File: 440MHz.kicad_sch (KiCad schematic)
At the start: 32 parts, among them J5 BWSMA-KWE-Z001, U7 GRF5604, U9 SKYA21003

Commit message: Finish up inputting things
Signed-off-by: Corey Minyard <corey@minyard.net>
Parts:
- removed C53: 0, Capacitor_SMD:C_0402_1005Metric_Pad0.74x0.62mm_HandSolder, symbol Device:C
- added C38: 5.1pF, Capacitor_SMD:C_0402_1005Metric_Pad0.74x0.62mm_HandSolder, symbol Device:C
- added C68: 2.2pF, Capacitor_SMD:C_0402_1005Metric_Pad0.74x0.62mm_HandSolder, symbol Device:C
- added C69: 0, Capacitor_SMD:C_0402_1005Metric_Pad0.74x0.62mm_HandSolder, symbol Device:C
- added L17: 27nH, Inductor_SMD:L_1210_3225Metric_Pad1.42x2.65mm_HandSolder, symbol Device:L
- added L19: 15nH, Inductor_SMD:L_1210_3225Metric_Pad1.42x2.65mm_HandSolder, symbol Device:L
- C50: value 18pF -> 15pF
- C51: value 18pF -> 5.1pF
- C52: value 33pF -> 2.2pF
- C55, C67: value 680pF -> 100pF
- C57: value 680pF -> 10pF
- C58: value 680pF -> 33pF
- C59, C60, C65: value 12pF -> 1000pF
- C61: value 12pF -> 33pF
- C62: value 12pF -> 2pF
- C63: value 12pF -> 10uF
- C64: value 12pF -> 28pF
- C66: value 12pF -> 1.8pF
- L10: value 47nH -> 43nH
- L11: value 82nH -> 27nH
- L12: value 68nH -> 22nH
- L13: value 68nH -> 10nH
- L14: value 68nH -> 23nH
- L15: value 68nH -> 2.2nH
- R11: value 56K 1% -> 1.96K 1%
- R12: value 56K 1% -> 6.04K 1%
- R13: value 56K 1% -> 0Ω
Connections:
- net 440MHz_RF_P is gone; now on net 440_RX_N: C51.2, L11.1, L9.2
- net 440_RX_P: now also L9.1, C38.1, L17.2
- net 440_TX: now also C68.1, L19.1; no longer C50.2, L10.1
- net GND: now also J5.3, L17.1
- net at C52.2, L10.2, L12.1: now also C69.1
- net 440MHz_TX_ENABLE: now reaches U7.1 (~{VSHUTDOWN})
- net at C54.2, C56.1, L12.2: now also C69.2
- net at C55.1, L11.2: now also C38.2
- new net: C50.2, C68.2, L10.1, L19.2
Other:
- moved on the sheet: C51, C58

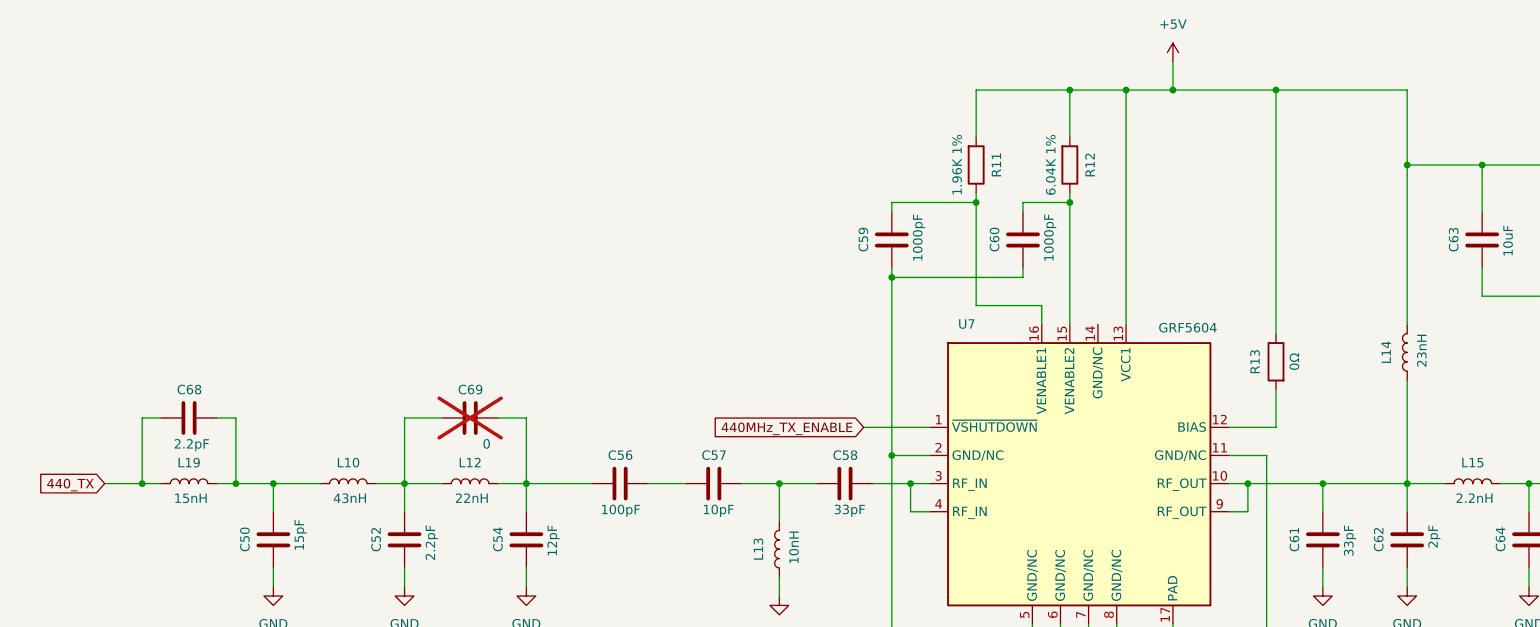
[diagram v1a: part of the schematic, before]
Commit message: Clean up schematics
Signed-off-by: Corey Minyard <corey@minyard.net>
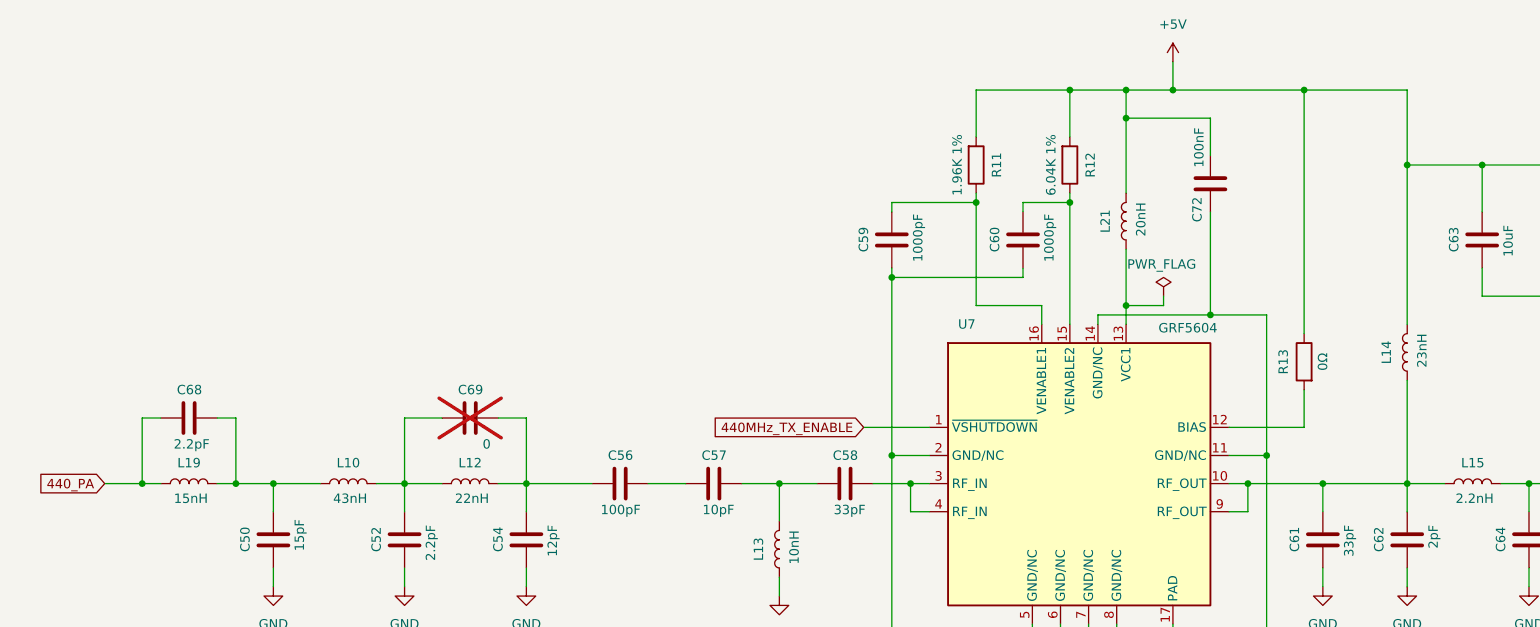
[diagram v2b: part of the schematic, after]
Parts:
- added C72: 100nF, Capacitor_SMD:C_0402_1005Metric_Pad0.74x0.62mm_HandSolder, symbol Device:C
- added L21: 20nH, Inductor_SMD:L_1210_3225Metric_Pad1.42x2.65mm_HandSolder, symbol Device:L
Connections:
- net +5V: now also C72.2, L21.2; no longer U7.13 (VCC1)
- net 440_TX: no longer C68.1, L19.1
- net GND: now also U7.14 (GND/NC), C72.1
- new net: L21.1, U7.13 (VCC1)
- new net 440_PA: C68.1, L19.1
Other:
- moved on the sheet: R13

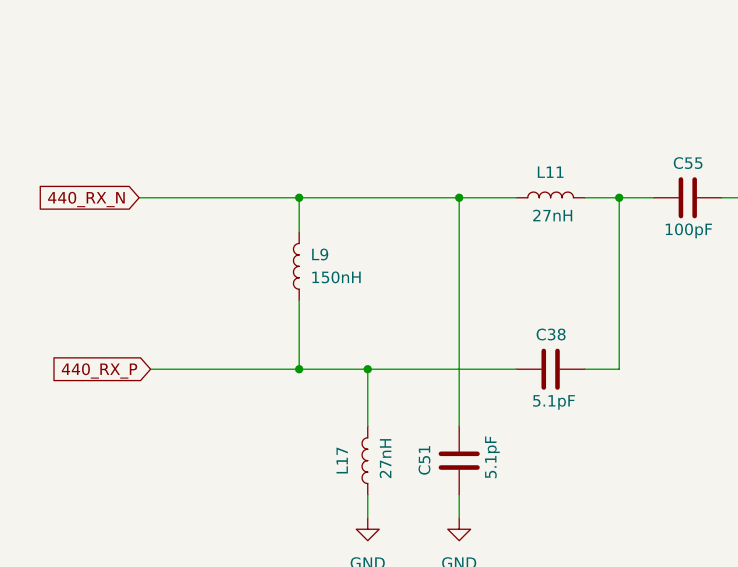
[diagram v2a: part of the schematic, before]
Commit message: More cleanups and add some test points
Signed-off-by: Corey Minyard <corey@minyard.net>
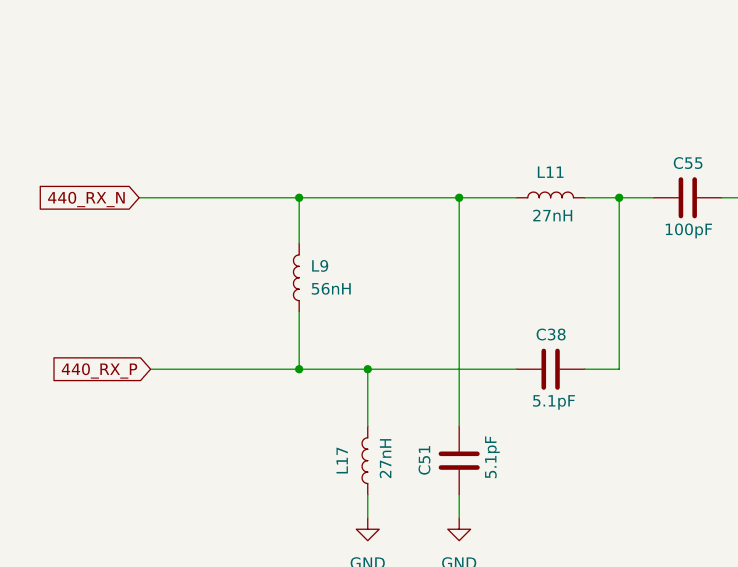
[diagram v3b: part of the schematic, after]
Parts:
- L10, L11, L12, L15, L17, L19, L21: footprint Inductor_SMD:L_1210_3225Metric_Pad1.42x2.65mm_HandSolder -> Inductor_SMD:L_0402_1005Metric_Pad0.77x0.64mm_HandSolder
- L14: footprint Inductor_SMD:L_1210_3225Metric_Pad1.42x2.65mm_HandSolder -> Inductor_SMD:L_0603_1608Metric_Pad1.05x0.95mm_HandSolder
- L9: value 150nH -> 56nH; footprint Inductor_SMD:L_1210_3225Metric_Pad1.42x2.65mm_HandSolder -> Inductor_SMD:L_0603_1608Metric_Pad1.05x0.95mm_HandSolder
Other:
- moved on the sheet: L9
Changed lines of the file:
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@@
 	(wire
 		(pts
-			(xy 54.61 139.7) (xy 54.61 147.32)
+			(xy 54.61 140.97) (xy 54.61 147.32)
 		)
 		(stroke
@@
 	(wire
 		(pts
-			(xy 54.61 128.27) (xy 54.61 132.08)
+			(xy 54.61 128.27) (xy 54.61 133.35)
 		)
 		(stroke
@@
 			)
 		)
-		(property "Footprint" "Inductor_SMD:L_1210_3225Metric_Pad1.42x2.65mm_HandSolder"
+		(property "Footprint" "Inductor_SMD:L_0603_1608Metric_Pad1.05x0.95mm_HandSolder"
 			(at 212.09 60.96 0)
 			(effects
@@
 			)
 		)
-		(property "Footprint" "Inductor_SMD:L_1210_3225Metric_Pad1.42x2.65mm_HandSolder"
+		(property "Footprint" "Inductor_SMD:L_0402_1005Metric_Pad0.77x0.64mm_HandSolder"
 			(at 68.58 78.74 0)
 			(effects
@@
 			)
 		)
-		(property "Footprint" "Inductor_SMD:L_1210_3225Metric_Pad1.42x2.65mm_HandSolder"
+		(property "Footprint" "Inductor_SMD:L_0402_1005Metric_Pad0.77x0.64mm_HandSolder"
 			(at 62.23 157.48 0)
 			(effects
@@
 			)
 		)
-		(property "Footprint" "Inductor_SMD:L_1210_3225Metric_Pad1.42x2.65mm_HandSolder"
+		(property "Footprint" "Inductor_SMD:L_0402_1005Metric_Pad0.77x0.64mm_HandSolder"
 			(at 46.99 78.74 0)
 			(effects
@@
 			)
 		)
-		(property "Footprint" "Inductor_SMD:L_1210_3225Metric_Pad1.42x2.65mm_HandSolder"
+		(property "Footprint" "Inductor_SMD:L_0402_1005Metric_Pad0.77x0.64mm_HandSolder"
 			(at 173.99 43.18 0)
 			(effects
@@
 			)
 		)
-		(property "Footprint" "Inductor_SMD:L_1210_3225Metric_Pad1.42x2.65mm_HandSolder"
+		(property "Footprint" "Inductor_SMD:L_0402_1005Metric_Pad0.77x0.64mm_HandSolder"
 			(at 82.55 128.27 0)
 			(effects
@@
 	(symbol
 		(lib_id "Device:L")
-		(at 54.61 135.89 180)
+		(at 54.61 137.16 180)
 		(unit 1)
 		(exclude_from_sim no)
@@
 		(fields_autoplaced yes)
 		(property "Reference" "L9"
-			(at 55.88 134.6199 0)
+			(at 55.88 135.8899 0)
 			(effects
 				(font
@@
 			)
 		)
-		(property "Value" "150nH"
-			(at 55.88 137.1599 0)
+		(property "Value" "56nH"
+			(at 55.88 138.4299 0)
 			(effects
 				(font
@@
 			)
 		)
-		(property "Footprint" "Inductor_SMD:L_1210_3225Metric_Pad1.42x2.65mm_HandSolder"
-			(at 54.61 135.89 0)
+		(property "Footprint" "Inductor_SMD:L_0603_1608Metric_Pad1.05x0.95mm_HandSolder"
+			(at 54.61 137.16 0)
 			(effects
 				(font
@@
 		)
 		(property "Datasheet" "~"
-			(at 54.61 135.89 0)
+			(at 54.61 137.16 0)
 			(effects
 				(font
@@
 		)
 		(property "Description" "Inductor"
-			(at 54.61 135.89 0)
+			(at 54.61 137.16 0)
 			(effects
 				(font
@@
 			)
 		)
-		(property "Footprint" "Inductor_SMD:L_1210_3225Metric_Pad1.42x2.65mm_HandSolder"
+		(property "Footprint" "Inductor_SMD:L_0402_1005Metric_Pad0.77x0.64mm_HandSolder"
 			(at 85.09 78.74 0)
 			(effects
@@
 			)
 		)
-		(property "Footprint" "Inductor_SMD:L_1210_3225Metric_Pad1.42x2.65mm_HandSolder"
+		(property "Footprint" "Inductor_SMD:L_0402_1005Metric_Pad0.77x0.64mm_HandSolder"
 			(at 220.98 78.74 0)
 			(effects

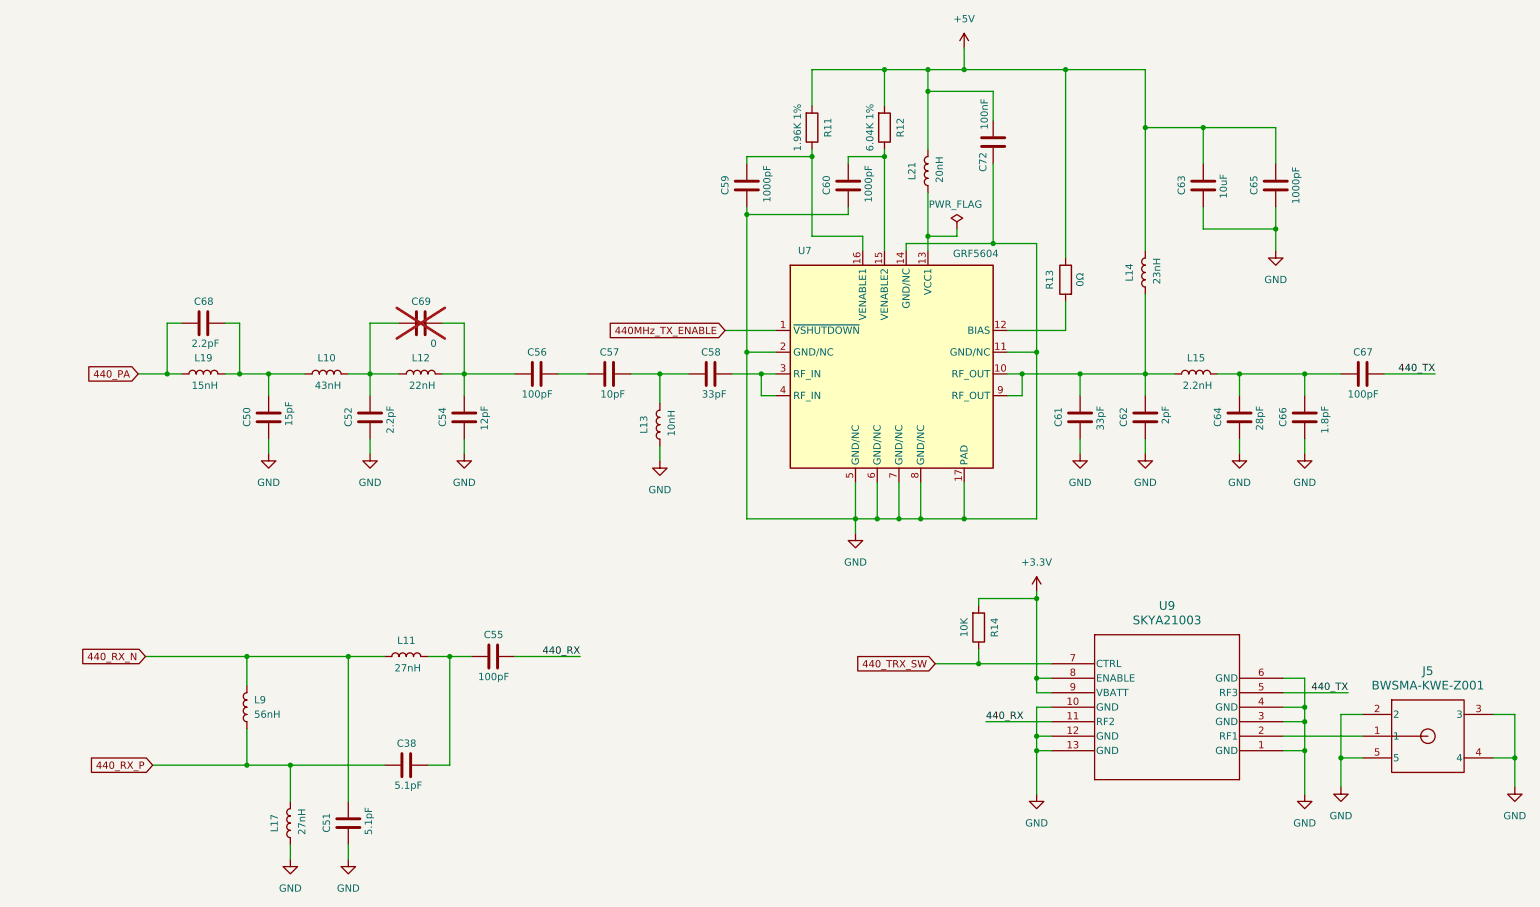
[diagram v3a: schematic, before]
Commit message: Add more test points
Signed-off-by: Corey Minyard <corey@minyard.net>
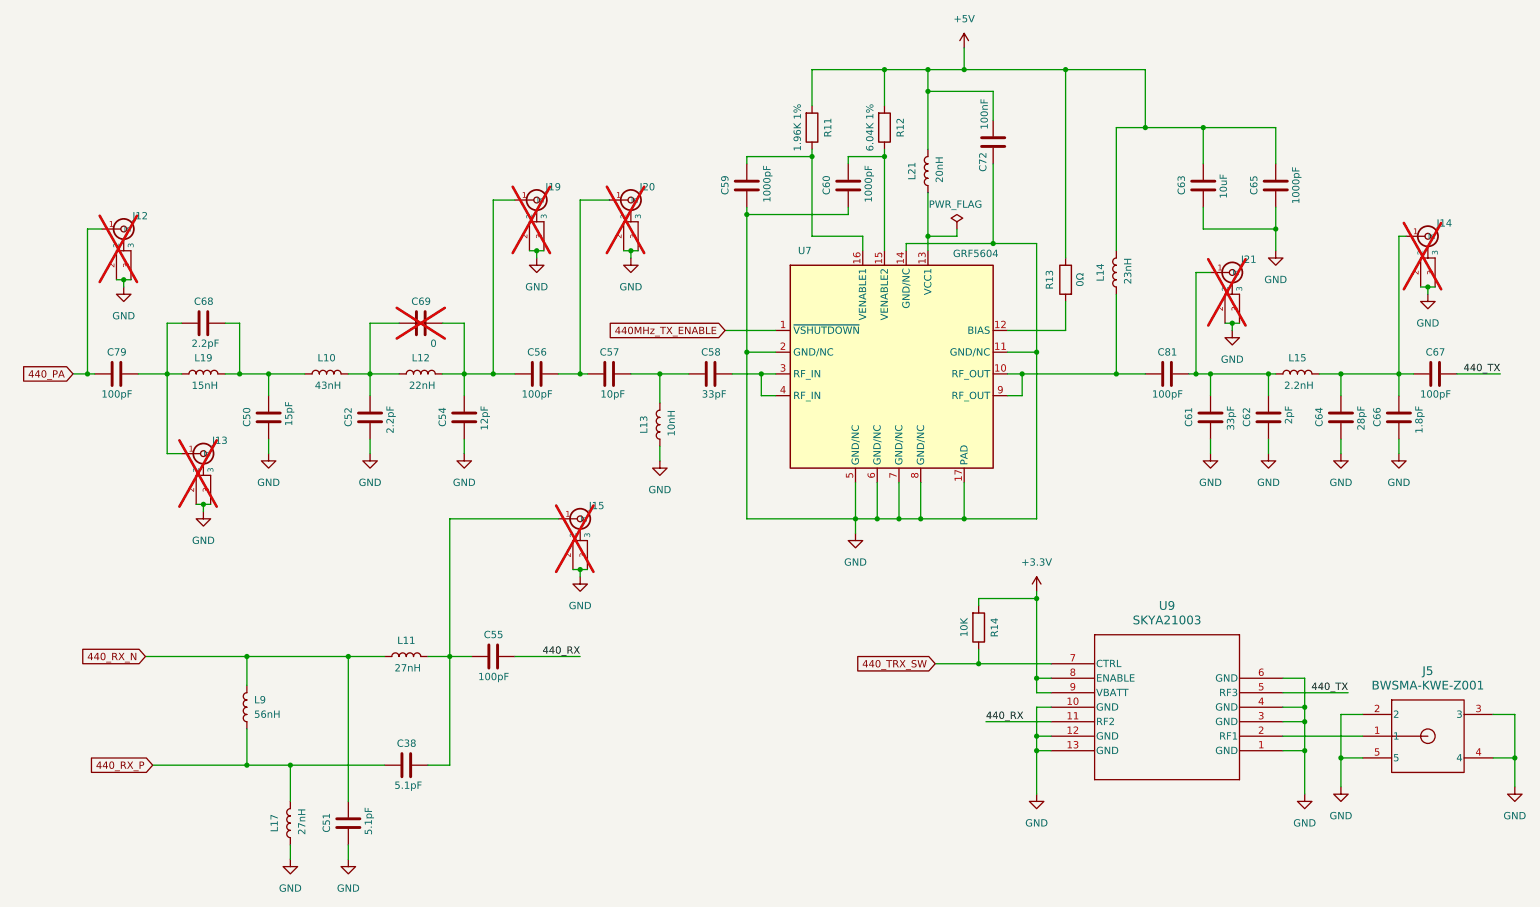
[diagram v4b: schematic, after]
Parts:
- added C79, C81: 100pF, Capacitor_SMD:C_0402_1005Metric_Pad0.74x0.62mm_HandSolder, symbol Device:C
- added J12, J13, J14, J15, J19, J20, J21: ~, footprints:CONN1_CONUFL_TEC, symbol Local Connectors:U_FL
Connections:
- net 440_PA: now also C79.1, J12.1 (In); no longer C68.1, L19.1
- net GND: now also J12.2, J12.3, J13.2, J13.3, J14.2, J14.3, J15.2, J15.3, J19.2, J19.3, J20.2, J20.3, J21.2, J21.3
- net at C38.2, C55.1, L11.2: now also J15.1 (In)
- net at L14.1, U7.10 (RF_OUT), U7.9 (RF_OUT): now also C81.1; no longer C61.2, C62.2, L15.1
- net at C64.2, C66.2, C67.1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: now also J14.1 (In)
- net at C54.2, C56.1, C69.2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: now also J19.1 (In)
- net at C56.2, C57.1: now also J20.1 (In)
- new net: C61.2, C62.2, C81.2, J21.1 (In), L15.1
- new net: C68.1, C79.2, J13.1 (In), L19.1
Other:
- moved on the sheet: C61, C62, C64, C66, C67, L14, L15

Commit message: Start on PCB
Clean up a lot of issues.

Signed-off-by: Corey Minyard <corey@minyard.net>
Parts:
- L13: footprint Inductor_SMD:L_1210_3225Metric_Pad1.42x2.65mm_HandSolder -> Inductor_SMD:L_0402_1005Metric_Pad0.77x0.64mm_HandSolder
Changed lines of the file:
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@@
 			)
 		)
-		(property "Footprint" "Inductor_SMD:L_1210_3225Metric_Pad1.42x2.65mm_HandSolder"
+		(property "Footprint" "Inductor_SMD:L_0402_1005Metric_Pad0.77x0.64mm_HandSolder"
 			(at 127 87.63 0)
 			(effects

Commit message: Layout work
Signed-off-by: Corey Minyard <corey@minyard.net>
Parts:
- added U10: 74LVC1GU04DRL, Package_TO_SOT_SMD:SOT-553, symbol 74xGxx:74LVC1GU04DRL
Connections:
- net +3.3V: now also U10.5 (VCC)
- net 440_RX: now also U9.5 (RF3); no longer U9.11 (RF2)
- net 440_TRX_SW: now also U10.2; no longer U9.7 (CTRL)
- net 440_TX: now also U9.11 (RF2); no longer U9.5 (RF3)
- net GND: now also U10.3 (GND)
- new net: U10.4, U9.7 (CTRL)
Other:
- moved on the sheet: R14

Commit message: Finish layout
Signed-off-by: Corey Minyard <corey@minyard.net>
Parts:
- C63: footprint Capacitor_SMD:C_0402_1005Metric_Pad0.74x0.62mm_HandSolder -> Capacitor_SMD:C_0805_2012Metric_Pad1.18x1.45mm_HandSolder
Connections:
- net RF_440: now reaches J5.1, U9.2 (RF1)
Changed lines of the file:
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@@
 	)
 	(junction
+		(at 243.84 142.24)
+		(diameter 0)
+		(color 0 0 0 0)
+	)
+	(junction
 		(at 76.2 78.74)
 		(diameter 0)
@@
 	(wire
 		(pts
+			(xy 265.43 161.29) (xy 243.84 161.29)
+		)
+		(stroke
+			(width 0)
+			(type default)
+		)
+	)
+	(wire
+		(pts
 			(xy 142.24 50.8) (xy 142.24 74.93)
 		)
@@
 	(wire
 		(pts
+			(xy 243.84 142.24) (xy 250.19 142.24)
+		)
+		(stroke
+			(width 0)
+			(type default)
+		)
+	)
+	(wire
+		(pts
 			(xy 146.05 129.54) (xy 154.94 129.54)
 		)
@@
 	(wire
 		(pts
+			(xy 243.84 161.29) (xy 243.84 142.24)
+		)
+		(stroke
+			(width 0)
+			(type default)
+		)
+	)
+	(wire
+		(pts
 			(xy 50.8 69.85) (xy 53.34 69.85)
 		)
@@
 	(wire
 		(pts
-			(xy 236.22 142.24) (xy 250.19 142.24)
+			(xy 236.22 142.24) (xy 243.84 142.24)
 		)
 		(stroke
@@
 		)
 	)
+	(global_label "RF_440"
+		(shape input)
+		(at 265.43 161.29 0)
+		(fields_autoplaced yes)
+		(effects
+			(font
+				(size 1.27 1.27)
+			)
+			(justify left)
+		)
+		(property "Intersheetrefs" "${INTERSHEET_REFS}"
+			(at 275.3699 161.29 0)
+			(effects
+				(font
+					(size 1.27 1.27)
+				)
+				(justify left)
+				(hide yes)
+			)
+		)
+	)
 	(global_label "440_PA"
 		(shape input)
@@
 			)
 		)
-		(property "Footprint" "Capacitor_SMD:C_0402_1005Metric_Pad0.74x0.62mm_HandSolder"
+		(property "Footprint" "Capacitor_SMD:C_0805_2012Metric_Pad1.18x1.45mm_HandSolder"
 			(at 221.2848 41.91 0)
 			(effects
@@
 		(on_board yes)
 		(dnp no)
-		(fields_autoplaced yes)
 		(property "Reference" "U10"
-			(at 186.69 123.1198 0)
+			(at 175.006 121.158 0)
 			(effects
 				(font
@@
 		)
 		(property "Value" "74LVC1GU04DRL"
-			(at 186.69 125.6598 0)
+			(at 175.006 123.698 0)
 			(effects
 				(font
